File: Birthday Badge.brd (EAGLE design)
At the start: 84.4 x 42.1 mm, 15 parts, among them Q1 2N2222, Q2 2N2222, Q3 2N2222

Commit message: Added back side text.
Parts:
- added U$1: (no value), n5ebw:OSHW1
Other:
- board text added: "Created by Ian Lee, Sr."
- board text added: "Happy 6th birthday Zander!"
- board text added: "http://ianlee.info"
- board text added: "ian@houseoflees.net"
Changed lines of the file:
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@@
 <wire x1="86.0425" y1="35.8775" x2="87.63" y2="35.8775" width="1.016" layer="121"/>
 <wire x1="21.2725" y1="36.195" x2="22.5425" y2="36.195" width="1.016" layer="121"/>
+<text x="67.31" y="33.655" size="1.778" layer="16" rot="MR0">Created by Ian Lee, Sr.</text>
+<text x="63.8175" y="31.115" size="1.778" layer="16" rot="MR0">http://ianlee.info</text>
+<text x="66.9925" y="28.575" size="1.778" layer="16" rot="MR0">ian@houseoflees.net</text>
+<text x="69.215" y="37.1475" size="1.778" layer="122" rot="SMR0">Happy 6th birthday Zander!</text>
 </plain>
 <attributes>
@@
 <attribute name="VALUE" x="61.30108125" y="18.55181875" size="1.016" layer="27" rot="R180"/>
 </element>
+<element name="U$1" library="n5ebw" package="OSHW1" value="" x="85.725" y="28.2575" rot="MR0"/>
 </elements>
 <signals>

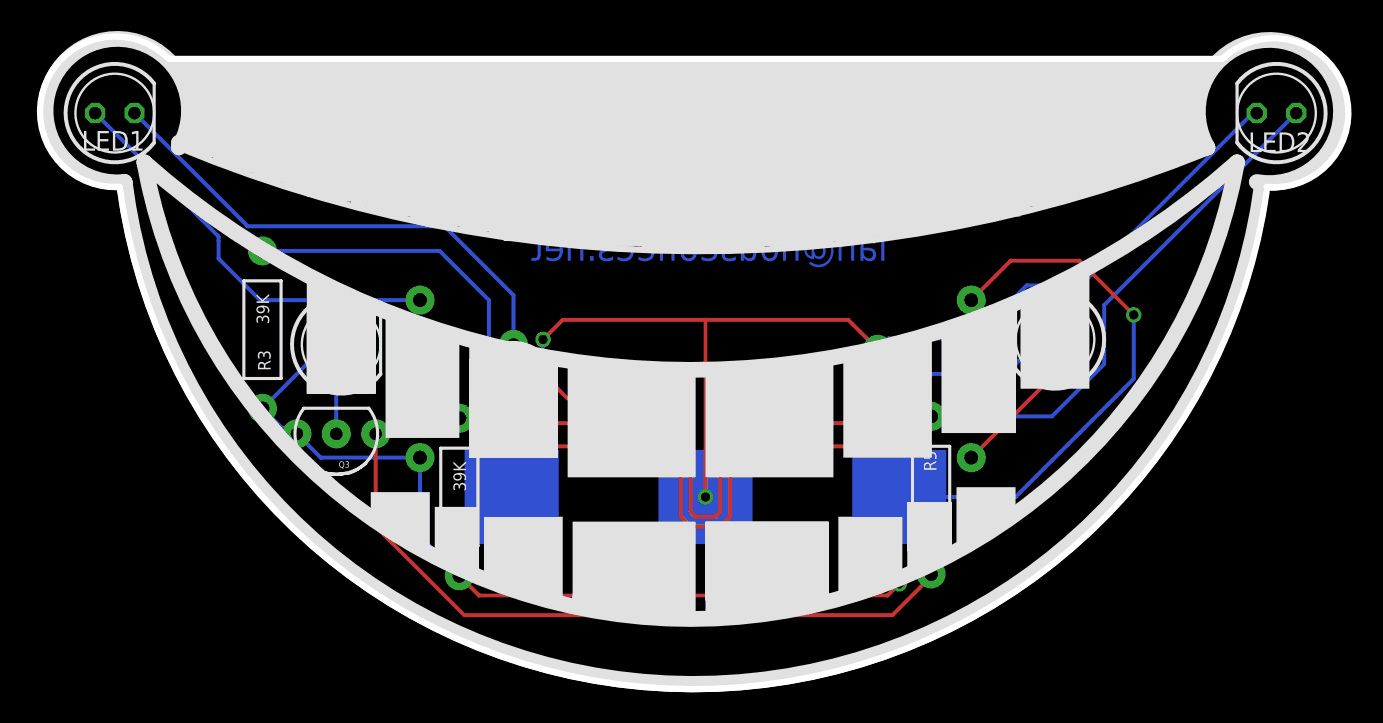
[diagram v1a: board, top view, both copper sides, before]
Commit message: Fixed transistor that was overlapping battery holder.
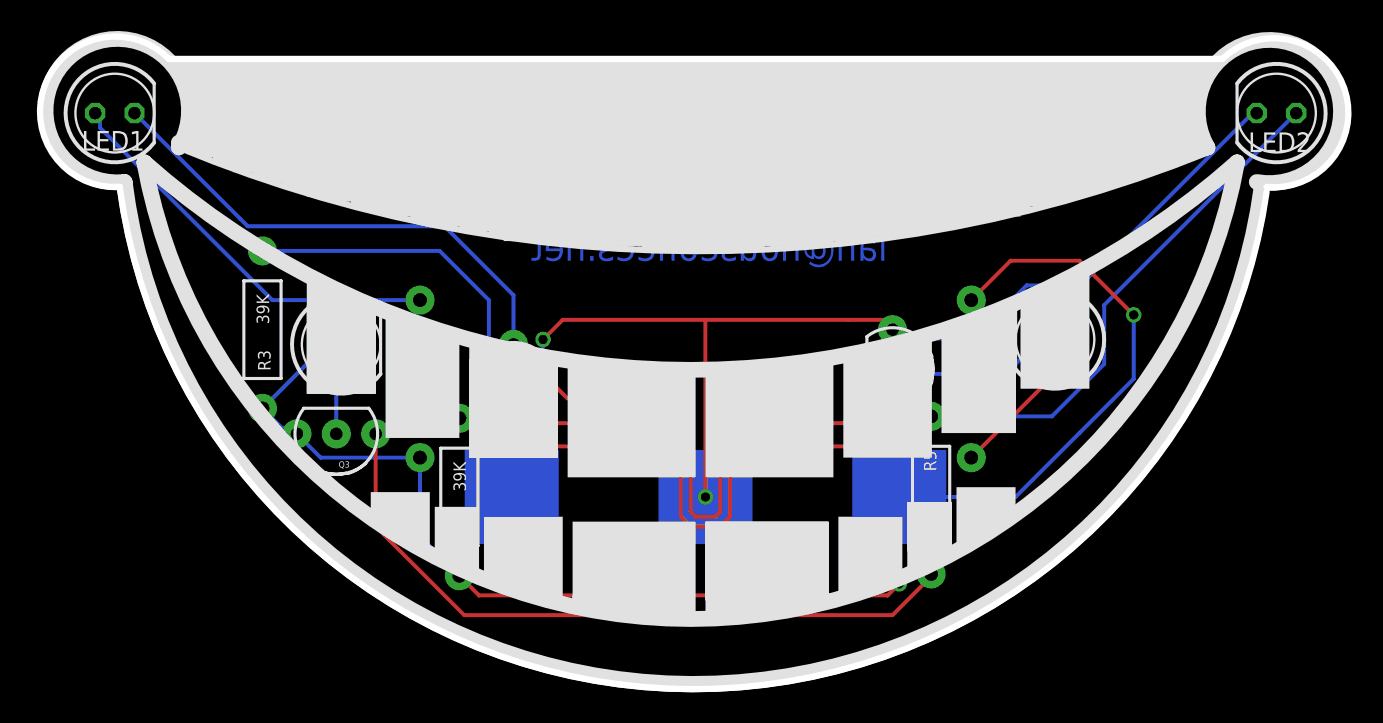
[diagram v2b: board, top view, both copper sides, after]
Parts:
- moved U$1 2.56 mm to (83.5, 29.5)
- moved Q2 1.59 mm to (67.3, 21.6)
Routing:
- net N$10: track 39.0 -> 40.5 mm
- net N$5: track 71.3 -> 70.7 mm
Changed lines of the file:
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@@
 <layer number="107" name="Crop" color="7" fill="1" visible="yes" active="yes"/>
 <layer number="116" name="Patch_BOT" color="9" fill="4" visible="yes" active="yes"/>
-<layer number="121" name="_tsilk" color="7" fill="1" visible="yes" active="yes"/>
+<layer number="121" name="_tsilk" color="7" fill="1" visible="no" active="yes"/>
 <layer number="122" name="_bsilk" color="7" fill="1" visible="yes" active="yes"/>
 <layer number="125" name="_tNames" color="7" fill="1" visible="yes" active="yes"/>
@@
 <text x="63.8175" y="31.115" size="1.778" layer="16" rot="MR0">http://ianlee.info</text>
 <text x="66.9925" y="28.575" size="1.778" layer="16" rot="MR0">ian@houseoflees.net</text>
-<text x="69.215" y="37.1475" size="1.778" layer="122" rot="SMR0">Happy 6th birthday Zander!</text>
+<text x="69.215" y="37.1475" size="1.778" layer="16" rot="SMR0">Happy 6th birthday Zander!</text>
 </plain>
 <attributes>
@@
 <attribute name="VALUE" x="41.3619625" y="19.851853125" size="0.4064" layer="27" ratio="10" rot="R90"/>
 </element>
-<element name="Q2" library="SparkFun" package="TO-92-AMMO" value="2N2222" x="66.3575" y="20.32" smashed="yes" rot="R270">
-<attribute name="NAME" x="68.2625" y="20.762390625" size="0.4064" layer="25" ratio="10" rot="R270"/>
-<attribute name="VALUE" x="67.646840625" y="21.264071875" size="0.4064" layer="27" ratio="10" rot="R270"/>
+<element name="Q2" library="SparkFun" package="TO-92-AMMO" value="2N2222" x="67.31" y="21.59" smashed="yes" rot="R270">
+<attribute name="NAME" x="69.215" y="22.032390625" size="0.4064" layer="25" ratio="10" rot="R270"/>
+<attribute name="VALUE" x="68.599340625" y="22.534071875" size="0.4064" layer="27" ratio="10" rot="R270"/>
 </element>
 <element name="Q3" library="SparkFun" package="TO-92-AMMO" value="2N2222" x="31.4325" y="17.40969375" smashed="yes" rot="R180">
@@
 <attribute name="VALUE" x="61.30108125" y="18.55181875" size="1.016" layer="27" rot="R180"/>
 </element>
-<element name="U$1" library="n5ebw" package="OSHW1" value="" x="85.725" y="28.2575" rot="MR0"/>
+<element name="U$1" library="n5ebw" package="OSHW1" value="" x="83.5025" y="29.5275" rot="MR0"/>
 </elements>
 <signals>
@@
 <wire x1="67.745" y1="7.7375" x2="67.745" y2="13.335" width="0.254" layer="16"/>
 <via x="67.745" y="7.7375" extent="1-16" drill="0.6"/>
-<wire x1="28.8925" y1="17.40969375" x2="28.575" y2="17.78" width="0" layer="19" extent="16-16"/>
 <wire x1="26.67" y1="19.05" x2="30.48" y2="22.86" width="0.254" layer="16"/>
 <wire x1="30.48" y1="22.86" x2="30.48" y2="23.1775" width="0.254" layer="16"/>
+<wire x1="28.575" y1="17.78" x2="28.8925" y2="17.40969375" width="0.1524" layer="16"/>
 </signal>
 <signal name="N$4">
@@
 <contactref element="R1" pad="P$1"/>
 <contactref element="LED1" pad="A"/>
-<wire x1="15.875" y1="38.1" x2="23.837009375" y2="30.137990625" width="0.254" layer="16"/>
-<wire x1="23.837009375" y1="30.137990625" x2="23.837009375" y2="29.861134375" width="0.254" layer="16"/>
-<wire x1="23.837009375" y1="29.861134375" x2="23.837009375" y2="28.710521875" width="0.254" layer="16"/>
-<wire x1="23.837009375" y1="28.710521875" x2="26.51253125" y2="26.035" width="0.254" layer="16"/>
-<wire x1="26.51253125" y1="26.035" x2="36.83" y2="26.035" width="0.254" layer="16"/>
+<wire x1="36.83" y1="26.035" x2="27.305" y2="26.035" width="0.254" layer="16"/>
+<wire x1="27.305" y1="26.035" x2="16.1925" y2="37.1475" width="0.254" layer="16"/>
+<wire x1="16.1925" y1="37.1475" x2="16.1925" y2="37.7825" width="0.254" layer="16"/>
+<wire x1="16.1925" y1="37.7825" x2="15.875" y2="38.1" width="0.254" layer="16"/>
 </signal>
 <signal name="N$7">
@@
 <contactref element="Q2" pad="3"/>
 <contactref element="C1" pad="1"/>
-<wire x1="66.3575" y1="17.78" x2="69.85" y2="21.2725" width="0.254" layer="16"/>
+<wire x1="67.31" y1="19.05" x2="69.85" y2="21.2725" width="0.254" layer="16"/>
 <wire x1="69.85" y1="21.2725" x2="74.6125" y2="21.2725" width="0.254" layer="16"/>
 <wire x1="74.6125" y1="21.2725" x2="76.5175" y2="23.1775" width="0.254" layer="16"/>
 <wire x1="76.5175" y1="23.1775" x2="76.5175" y2="23.495" width="0.254" layer="16"/>
-<wire x1="59.3725" y1="16.5975" x2="64.2225" y2="16.5975" width="0.254" layer="1"/>
-<wire x1="64.2225" y1="16.5975" x2="64.4525" y2="16.8275" width="0.254" layer="1"/>
-<wire x1="64.4525" y1="16.8275" x2="65.405" y2="17.78" width="0.254" layer="1"/>
-<wire x1="65.405" y1="17.78" x2="66.3575" y2="17.78" width="0.254" layer="1"/>
+<wire x1="59.3725" y1="16.5975" x2="64.8575" y2="16.5975" width="0.254" layer="1"/>
+<wire x1="64.8575" y1="16.5975" x2="67.31" y2="19.05" width="0.254" layer="1"/>
 </signal>
 <signal name="N$10">
@@
 <wire x1="56.8325" y1="17.4625" x2="57.4675" y2="18.0975" width="0.254" layer="1"/>
 <wire x1="62.23" y1="18.0975" x2="64.135" y2="18.0975" width="0.254" layer="1"/>
-<wire x1="64.135" y1="18.0975" x2="66.3575" y2="20.32" width="0.254" layer="1"/>
+<wire x1="64.135" y1="18.0975" x2="67.31" y2="21.59" width="0.254" layer="1"/>
 </signal>
 <signal name="N$11">
@@
 <contactref element="CR2032" pad="2"/>
 <contactref element="LED2" pad="K"/>
-<wire x1="66.3575" y1="22.86" x2="67.060178125" y2="23.562678125" width="0.254" layer="16"/>
-<wire x1="67.060178125" y1="23.562678125" x2="72.542246875" y2="23.562678125" width="0.254" layer="16"/>
 <wire x1="72.542246875" y1="23.562678125" x2="75.96705625" y2="26.9874875" width="0.254" layer="16"/>
 <wire x1="75.96705625" y1="26.9874875" x2="79.4358125" y2="26.9874875" width="0.254" layer="16"/>
@@
 <via x="44.7675" y="23.495" extent="1-16" drill="0.6"/>
 <wire x1="55.245" y1="24.765" x2="64.4525" y2="24.765" width="0.254" layer="1"/>
-<wire x1="64.4525" y1="24.765" x2="66.3575" y2="22.86" width="0.254" layer="1"/>
+<wire x1="64.4525" y1="24.765" x2="66.675" y2="24.765" width="0.254" layer="1"/>
+<wire x1="66.675" y1="24.765" x2="67.31" y2="24.13" width="0.254" layer="1"/>
+<wire x1="72.542246875" y1="23.562678125" x2="67.877321875" y2="23.562678125" width="0.254" layer="16"/>
+<wire x1="67.877321875" y1="23.562678125" x2="67.31" y2="24.13" width="0.254" layer="16"/>
 </signal>
 <signal name="N$3">

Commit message: Adjusted text locations after viewing created Gerber files.
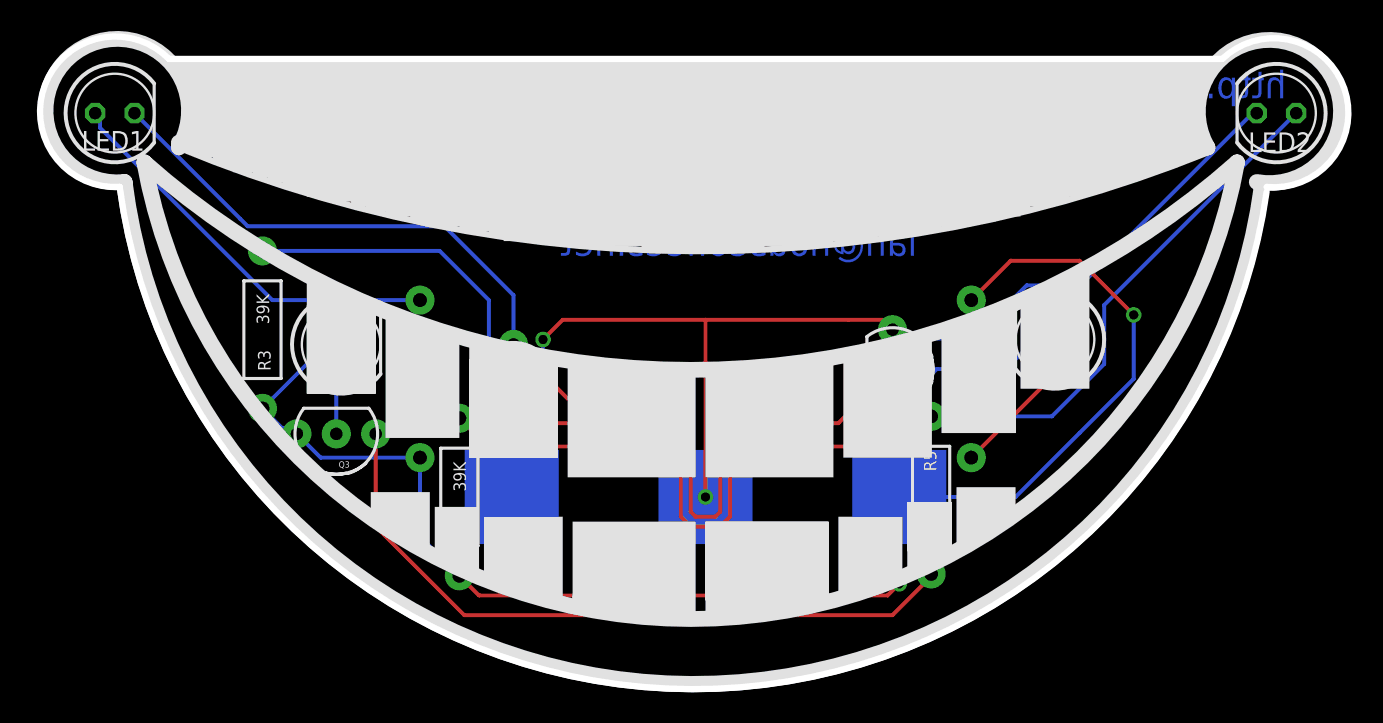
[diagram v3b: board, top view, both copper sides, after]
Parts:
- moved U$1 3.14 mm to (81.3, 27.3)
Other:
- board text added: "http://blog.ianlee.info/2012/09/birthday-badge.html"
- board text removed: "http://ianlee.info"
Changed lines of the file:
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@@
 <layer number="27" name="tValues" color="7" fill="1" visible="yes" active="yes"/>
 <layer number="28" name="bValues" color="7" fill="1" visible="yes" active="yes"/>
-<layer number="29" name="tStop" color="7" fill="3" visible="no" active="yes"/>
-<layer number="30" name="bStop" color="7" fill="6" visible="no" active="yes"/>
+<layer number="29" name="tStop" color="7" fill="3" visible="yes" active="yes"/>
+<layer number="30" name="bStop" color="7" fill="6" visible="yes" active="yes"/>
 <layer number="31" name="tCream" color="7" fill="4" visible="yes" active="yes"/>
 <layer number="32" name="bCream" color="7" fill="5" visible="yes" active="yes"/>
@@
 <wire x1="86.0425" y1="35.8775" x2="87.63" y2="35.8775" width="1.016" layer="121"/>
 <wire x1="21.2725" y1="36.195" x2="22.5425" y2="36.195" width="1.016" layer="121"/>
-<text x="67.31" y="33.655" size="1.778" layer="16" rot="MR0">Created by Ian Lee, Sr.</text>
-<text x="63.8175" y="31.115" size="1.778" layer="16" rot="MR0">http://ianlee.info</text>
-<text x="66.9925" y="28.575" size="1.778" layer="16" rot="MR0">ian@houseoflees.net</text>
-<text x="69.215" y="37.1475" size="1.778" layer="16" rot="SMR0">Happy 6th birthday Zander!</text>
+<text x="69.85" y="32.0675" size="1.778" layer="16" rot="MR0">Created by Ian Lee, Sr.</text>
+<text x="68.8975" y="28.8925" size="1.778" layer="16" rot="MR0">ian@houseoflees.net</text>
+<text x="69.215" y="35.2425" size="1.778" layer="122" rot="SMR0">Happy 6th birthday Zander!</text>
+<text x="92.71" y="39.0525" size="1.778" layer="16" rot="MR0">http://blog.ianlee.info/2012/09/birthday-badge.html</text>
 </plain>
 <attributes>
@@
 <attribute name="VALUE" x="61.30108125" y="18.55181875" size="1.016" layer="27" rot="R180"/>
 </element>
-<element name="U$1" library="n5ebw" package="OSHW1" value="" x="83.5025" y="29.5275" rot="MR0"/>
+<element name="U$1" library="n5ebw" package="OSHW1" value="" x="81.28" y="27.305" rot="MR0"/>
 </elements>
 <signals>
@@
 <wire x1="79.375" y1="28.575" x2="74.93" y2="28.575" width="0.254" layer="1"/>
 <wire x1="74.93" y1="28.575" x2="72.39" y2="26.035" width="0.254" layer="1"/>
-<wire x1="28.8925" y1="17.40969375" x2="30.42719375" y2="15.875" width="0.254" layer="16"/>
 <wire x1="30.42719375" y1="15.875" x2="36.83" y2="15.875" width="0.254" layer="16"/>
 <wire x1="75.2475" y1="13.335" x2="67.745" y2="13.335" width="0.254" layer="16"/>
@@
 <wire x1="26.67" y1="19.05" x2="30.48" y2="22.86" width="0.254" layer="16"/>
 <wire x1="30.48" y1="22.86" x2="30.48" y2="23.1775" width="0.254" layer="16"/>
-<wire x1="28.575" y1="17.78" x2="28.8925" y2="17.40969375" width="0.1524" layer="16"/>
+<wire x1="28.575" y1="17.78" x2="28.8925" y2="17.40969375" width="0" layer="19" extent="1-16"/>
+<wire x1="30.42719375" y1="15.875" x2="28.8925" y2="17.40969375" width="0.254" layer="16"/>
 </signal>
 <signal name="N$4">
@@
 <contactref element="Q2" pad="3"/>
 <contactref element="C1" pad="1"/>
-<wire x1="67.31" y1="19.05" x2="69.85" y2="21.2725" width="0.254" layer="16"/>
-<wire x1="69.85" y1="21.2725" x2="74.6125" y2="21.2725" width="0.254" layer="16"/>
-<wire x1="74.6125" y1="21.2725" x2="76.5175" y2="23.1775" width="0.254" layer="16"/>
 <wire x1="76.5175" y1="23.1775" x2="76.5175" y2="23.495" width="0.254" layer="16"/>
 <wire x1="59.3725" y1="16.5975" x2="64.8575" y2="16.5975" width="0.254" layer="1"/>
 <wire x1="64.8575" y1="16.5975" x2="67.31" y2="19.05" width="0.254" layer="1"/>
+<wire x1="67.31" y1="19.05" x2="67.6275" y2="19.05" width="0.254" layer="16"/>
+<wire x1="67.6275" y1="19.05" x2="70.1675" y2="21.59" width="0.254" layer="16"/>
+<wire x1="70.1675" y1="21.59" x2="74.6125" y2="21.59" width="0.254" layer="16"/>
+<wire x1="74.6125" y1="21.59" x2="76.5175" y2="23.495" width="0.254" layer="16"/>
 </signal>
 <signal name="N$10">
@@
 <wire x1="56.8325" y1="12.065" x2="56.8325" y2="17.4625" width="0.254" layer="1"/>
 <wire x1="56.8325" y1="17.4625" x2="57.4675" y2="18.0975" width="0.254" layer="1"/>
-<wire x1="62.23" y1="18.0975" x2="64.135" y2="18.0975" width="0.254" layer="1"/>
-<wire x1="64.135" y1="18.0975" x2="67.31" y2="21.59" width="0.254" layer="1"/>
+<wire x1="62.23" y1="18.0975" x2="63.8175" y2="18.0975" width="0.254" layer="1"/>
+<wire x1="63.8175" y1="18.0975" x2="67.31" y2="21.59" width="0.254" layer="1"/>
 </signal>
 <signal name="N$11">
